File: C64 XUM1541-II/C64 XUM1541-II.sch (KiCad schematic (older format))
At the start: 19 parts, among them J1 C64_IEC, J2 SpeedDOS, M1 Mounting, M2 Mounting, M3 Mounting, M4 Mounting, SW1 RESET, U1 7406

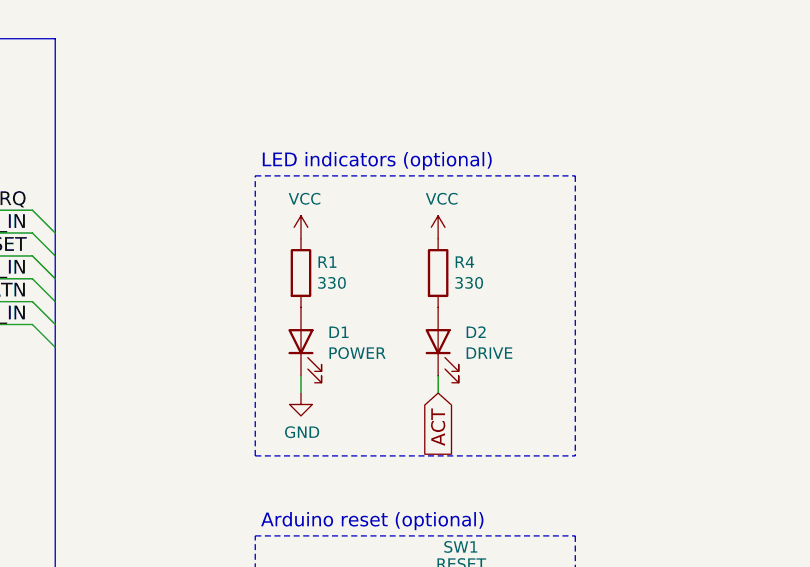
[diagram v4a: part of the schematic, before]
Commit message: Rotated parallel connector
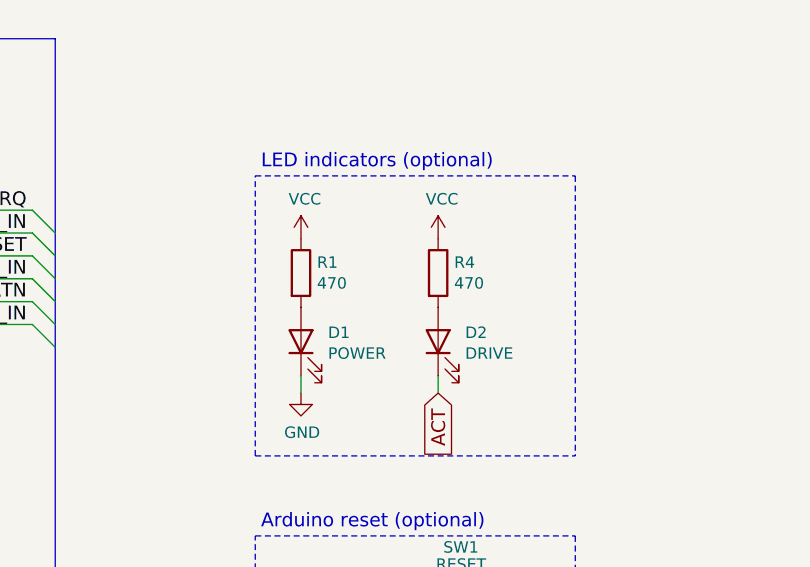
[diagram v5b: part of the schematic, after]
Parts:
- R1, R4: value 330 -> 470
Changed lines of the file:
@@
 P 9000 2025
 F 0 "R1" H 9070 2071 50  0000 L CNN
-F 1 "330" H 9070 1980 50  0000 L CNN
+F 1 "470" H 9070 1980 50  0000 L CNN
 F 2 "Resistor_THT:R_Axial_DIN0207_L6.3mm_D2.5mm_P10.16mm_Horizontal" V 8930 2025 50  0001 C CNN
 F 3 "~" H 9000 2025 50  0001 C CNN
@@
 P 9600 2025
 F 0 "R4" H 9670 2071 50  0000 L CNN
-F 1 "330" H 9670 1980 50  0000 L CNN
+F 1 "470" H 9670 1980 50  0000 L CNN
 F 2 "Resistor_THT:R_Axial_DIN0207_L6.3mm_D2.5mm_P10.16mm_Horizontal" V 9530 2025 50  0001 C CNN
 F 3 "~" H 9600 2025 50  0001 C CNN

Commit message: Updated gerber files and small tweaks
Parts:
- J1: value C64_IEC -> IEC
- J2: value SpeedDOS -> PARALLEL
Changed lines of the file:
@@
 P 2850 5075
 F 0 "J2" H 2850 5500 50  0000 C CNN
-F 1 "SpeedDOS" H 2850 5400 50  0000 C CNN
+F 1 "PARALLEL" H 2850 5400 50  0000 C CNN
 F 2 "speed_dos:SpeedDOS_IDC" H 2850 5075 50  0001 C CNN
 F 3 "~" H 2850 5075 50  0001 C CNN
@@
 P 6350 4625
 F 0 "J1" H 6075 5000 50  0000 C CNN
-F 1 "C64_IEC" H 6075 4925 50  0000 C CNN
+F 1 "IEC" H 6075 4925 50  0000 C CNN
 F 2 "C64_IEC:C64_IEC" H 6350 4625 50  0001 C CNN
 F 3 "http://www.mouser.com/ds/2/18/40_c091_abd_e-75918.pdf" H 6350 4625 50  0001 C CNN
